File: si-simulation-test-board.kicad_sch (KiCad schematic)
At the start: 28 parts, among them J1 Conn_SMA_RF2-143-T-17-50-G, J10 Conn_SMA_RF2-143-T-17-50-G, J11 Conn_SMA_RF2-143-T-17-50-G, J12 Conn_SMA_RF2-143-T-17-50-G, J13 Conn_SMA_RF2-143-T-17-50-G, J14 Conn_SMA_RF2-143-T-17-50-G, J15 Conn_SMA_RF2-143-T-17-50-G, J16 Conn_SMA_RF2-143-T-17-50-G, J17 Conn_SMA_RF2-143-T-17-50-G, J18 Conn_SMA_RF2-143-T-17-50-G, J19 Conn_SMA_RF2-143-T-17-50-G, J2 Conn_SMA_RF2-143-T-17-50-G, J20 Conn_SMA_RF2-143-T-17-50-G, J21 Conn_SMA_RF2-143-T-17-50-G, J22 Conn_SMA_RF2-143-T-17-50-G, J3 Conn_SMA_RF2-143-T-17-50-G, J4 Conn_SMA_RF2-143-T-17-50-G, J5 Conn_SMA_RF2-143-T-17-50-G, J6 Conn_SMA_RF2-143-T-17-50-G, J7 Conn_SMA_RF2-143-T-17-50-G, J8 Conn_SMA_RF2-143-T-17-50-G, J9 Conn_SMA_RF2-143-T-17-50-G

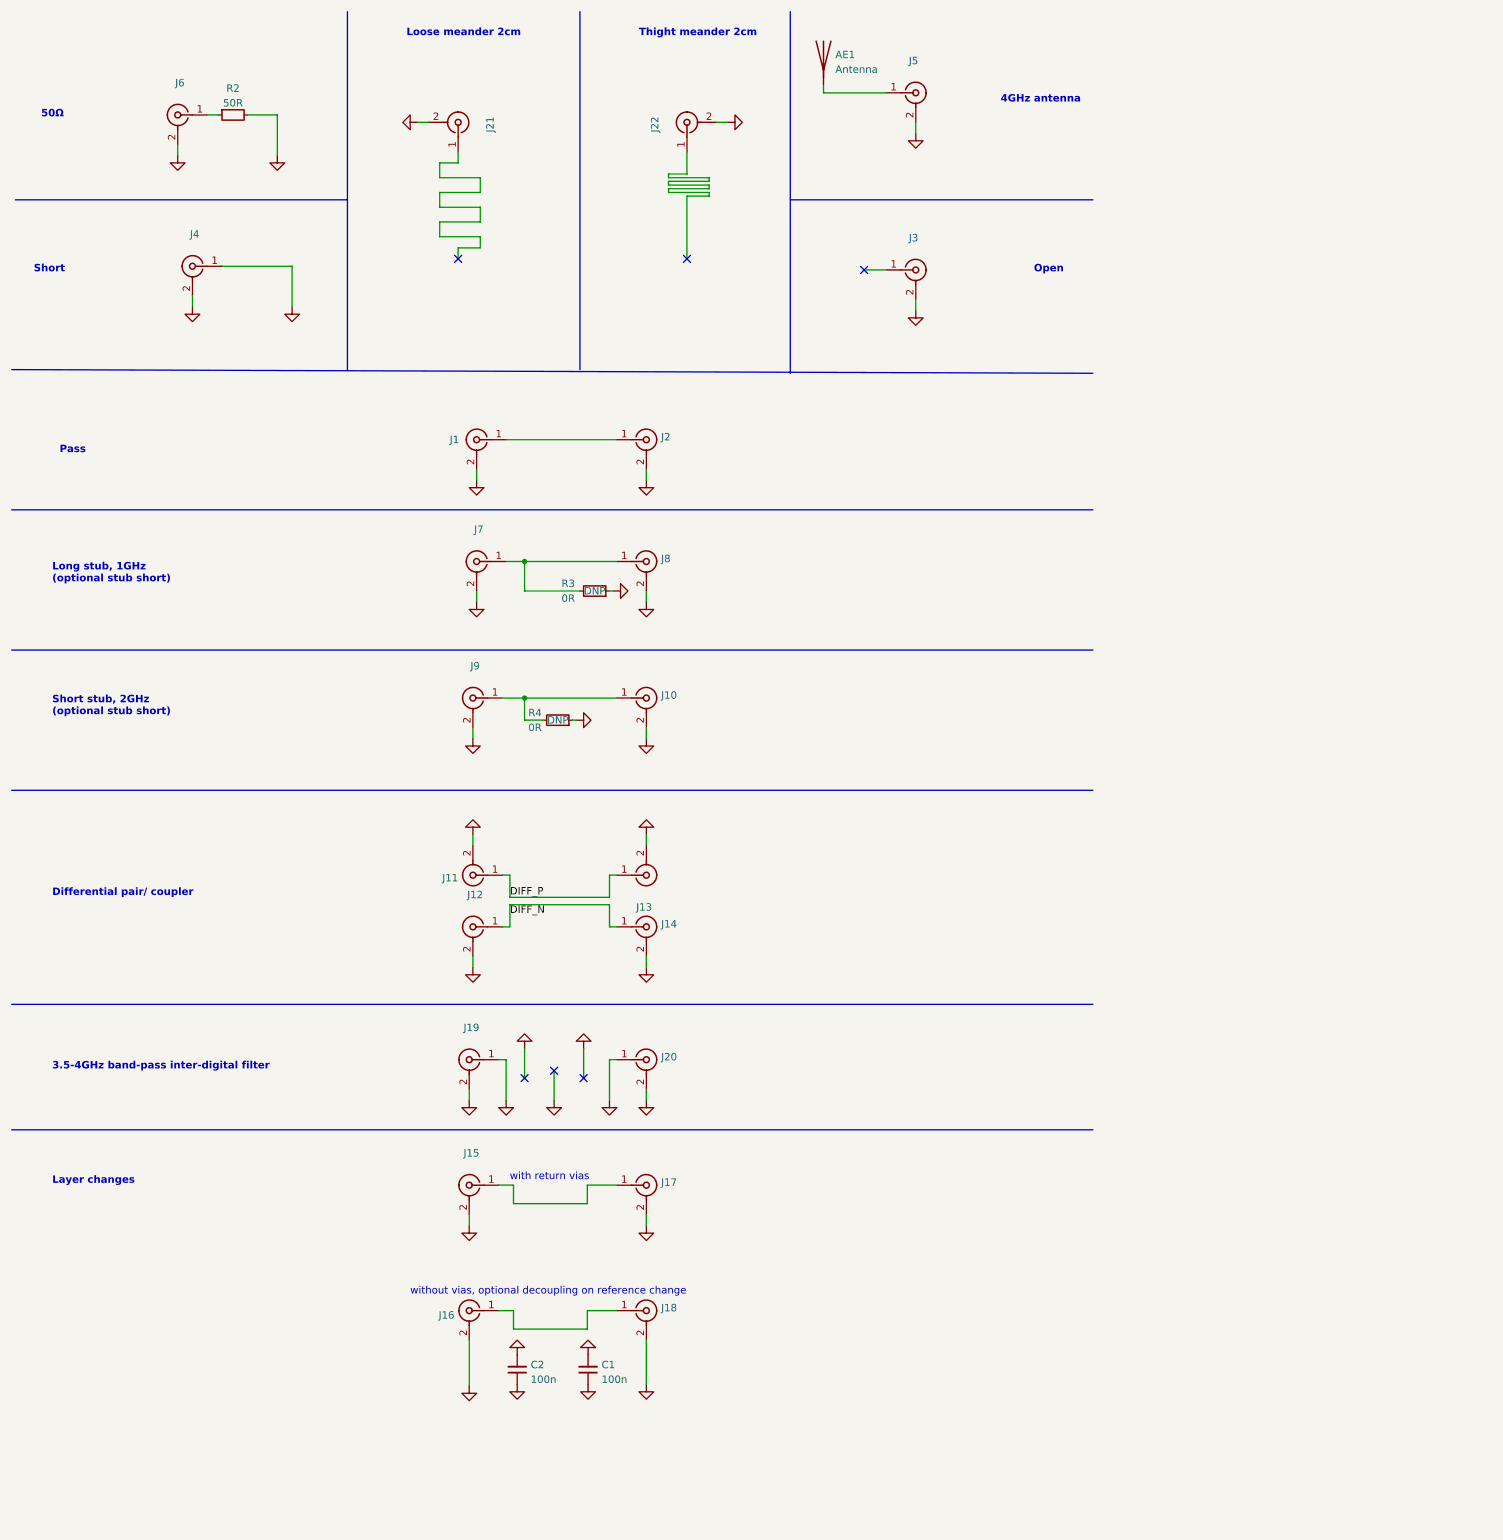
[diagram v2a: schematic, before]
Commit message: Make SCH A3 landscape
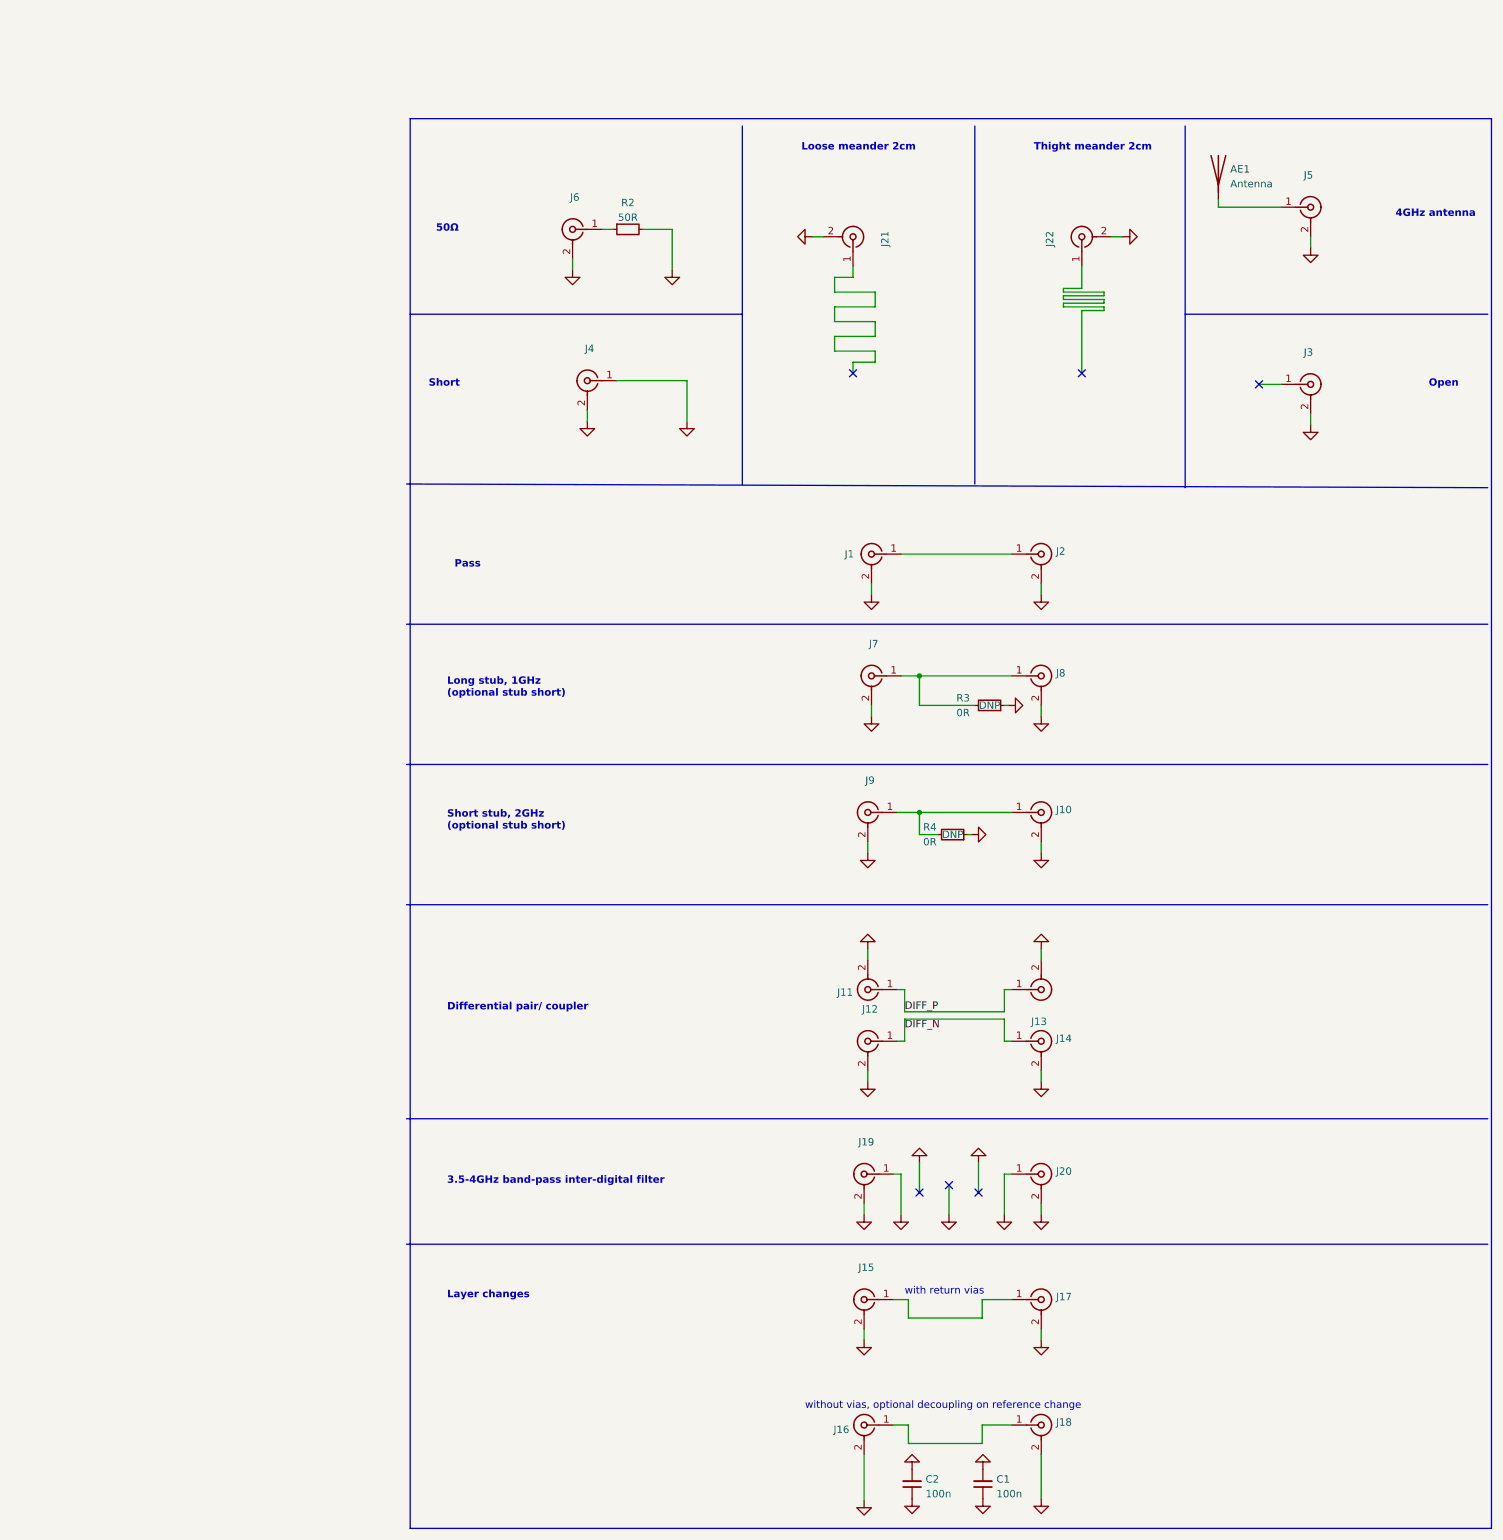
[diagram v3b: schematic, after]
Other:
- moved on the sheet: AE1, C1, C2, J1, J10, J11, J12, J13, J14, J15, J16, J17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

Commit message: Add local libraries
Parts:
- AE1: symbol Device:Antenna -> si-simulation-test-board:Antenna
- C1, C2: footprint antmicro-footprints:C_0402_1005Metric -> si-simulation-test-board-footprints:C_0402_1005Metric; symbol antmicroCapacitors0402:C_100n_0402 -> si-simulation-test-board:C_100n_0402
- J1, J10, J11, J12, J13, J14, J15, J16, J17, J18, J19, J2, J20, J21, J22, J3, J4, J5, J6, J7, J8, J9: footprint antmicro-footprints:RF_SMA_BoardEdge_RF2-143-T-17-50-G -> si-simulation-test-board-footprints:RF_SMA_BoardEdge_RF2-143-T-17-50-G; symbol antmicroCoaxialConnectorsRF:Conn_SMA_RF2-143-T-17-50-G -> si-simulation-test-board:Conn_SMA_RF2-143-T-17-50-G
- R2: footprint antmicro-footprints:R_0402_1005Metric -> si-simulation-test-board-footprints:R_0402_1005Metric; symbol antmicroResistors0402:R_50R_0402 -> si-simulation-test-board:R_50R_0402
- R3, R4: footprint antmicro-footprints:R_0201 -> si-simulation-test-board-footprints:R_0201; symbol antmicroResistorsmisc:R_0R_0201 -> si-simulation-test-board:R_0R_0201
